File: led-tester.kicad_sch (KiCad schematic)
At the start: 35 parts, among them M1 Arduino_Mini, Q1 MMBT3904, U1 PCF8591, U2 LMV358

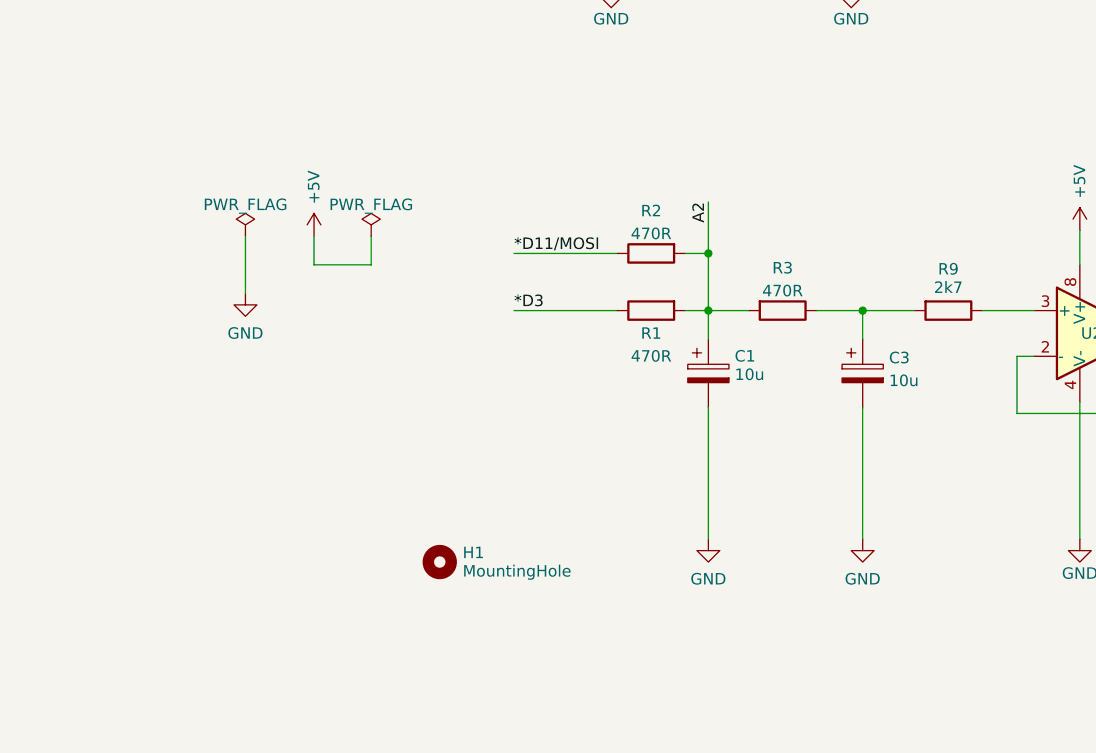
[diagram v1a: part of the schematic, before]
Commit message: News caps plus tweaks
Added SMD caps as alternatives to THT
Updated footprints from library
Separator on silk between power LED and test LEDs.
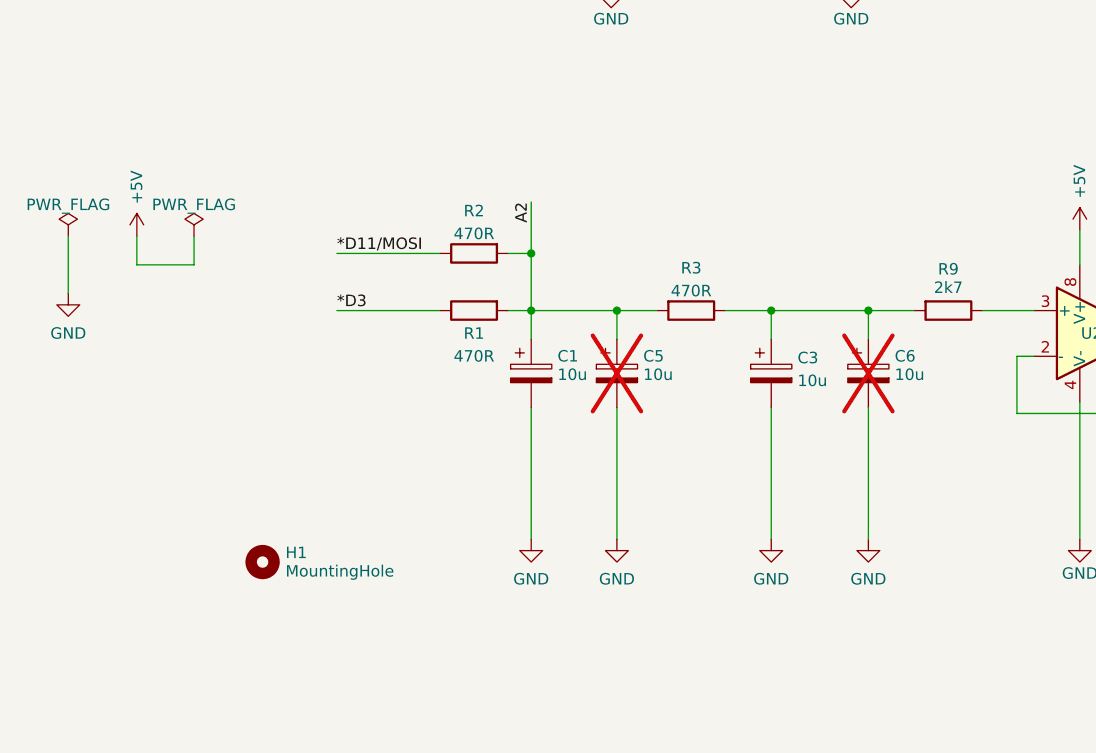
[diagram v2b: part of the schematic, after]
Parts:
- added C5, C6: 10u, Capacitor_SMD:C_0805_2012Metric_Pad1.18x1.45mm_HandSolder, symbol Device:C_Polarized
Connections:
- net A2: now also C5.1
- net GND: now also C5.2, C6.2
- net at C3.1, R3.1, R9.2: now also C6.1
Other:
- moved on the sheet: C1, C3, H1, R1, R2, R3
